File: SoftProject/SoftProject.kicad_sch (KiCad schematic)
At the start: 37 parts, among them J1 USB_B_Micro, Q1 2N2219, Q2 2N2219, SW1 SW_Push, SW2 SW_Push, U1 ESP32-S2-WROVER, U2 AMS1117, U3 CP2102N-Axx-xQFN28

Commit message: Finished schematic
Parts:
- added J2: Conn_01x21_Pin, symbol Connector:Conn_01x21_Pin
- added J4: Conn_01x19_Pin, symbol Connector:Conn_01x19_Pin
- added R13: R, symbol Device:R
- added R14, R15, R16, R17: 0, symbol Device:R
- C1, C14, C4, C7, C8, C9: value 0.1u -> 0.1uF
- C10, C2, C5, C6: value 10u -> 10uF
- C11, C12: value 22p -> 22pF
- C13: value 4.7u -> 4.7uF
- C3: value 1u -> 1uF
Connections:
- net +3.3V: now also J2.1 (Pin_1)
- net +5V: now also J2.20 (Pin_20)
- net CHIP_PU: now also J4.2 (Pin_2), R16.2
- net EN_Auto: now also R16.1
- net GND: now also J2.21 (Pin_21), J4.1 (Pin_1), J4.19 (Pin_19), R13.2
- net GPIO0: now also J2.2 (Pin_2), R17.2
- net GPIO1: now also J2.3 (Pin_3)
- net GPIO10: now also J2.12 (Pin_12)
- net GPIO11: now also J2.13 (Pin_13)
- net GPIO12: now also J2.14 (Pin_14)
- net GPIO13: now also J2.15 (Pin_15)
- net GPIO14: now also J2.16 (Pin_16)
- net GPIO15: now also J2.17 (Pin_17)
- net GPIO16: now also J2.18 (Pin_18)
- net GPIO17: now also J2.19 (Pin_19)
- net GPIO2: now also J2.4 (Pin_4)
- net GPIO3: now also J2.5 (Pin_5)
- net GPIO4: now also J2.6 (Pin_6)
- net GPIO5: now also J2.7 (Pin_7)
- net GPIO6: now also J2.8 (Pin_8)
- net GPIO7: now also J2.9 (Pin_9)
- net GPIO8: now also J2.10 (Pin_10)
- net GPIO9: now also J2.11 (Pin_11)
- net IO0_Auto: now also R17.1
- net RXD_CP: now also J4.5 (Pin_5), R15.2
- net TXD_CP: now also J4.6 (Pin_6), R14.2
- net USB_DN: now also U1.22 (USB_D-)
- net USB_DP: now also U1.23 (USB_D+)
- net at U3.11 (~{SUSPEND}): now also R13.1
- net GPIO21: now reaches U1.24 (IO21)
- net GPIO21: now also J4.18 (Pin_18)
- net GPIO26: now reaches U1.25 (IO26)
- net GPIO26: now also J4.17 (Pin_17)
- net GPIO33: now reaches U1.27 (IO33)
- net GPIO33: now also J4.16 (Pin_16)
- net GPIO34: now reaches U1.28 (IO34)
- net GPIO34: now also J4.15 (Pin_15)
- net GPIO35: now reaches U1.29 (IO35)
- net GPIO35: now also J4.14 (Pin_14)
- net GPIO36: now reaches U1.30 (IO36)
- net GPIO36: now also J4.13 (Pin_13)
- net GPIO37: now reaches U1.31 (IO37)
- net GPIO37: now also J4.12 (Pin_12)
- net GPIO38: now reaches U1.32 (IO38)
- net GPIO38: now also J4.11 (Pin_11)
- net GPIO39: now reaches U1.33 (IO39)
- net GPIO39: now also J4.10 (Pin_10)
- net GPIO40: now reaches U1.34 (IO40)
- net GPIO40: now also J4.9 (Pin_9)
- net GPIO41: now reaches U1.35 (IO41)
- net GPIO41: now also J4.8 (Pin_8)
- net GPIO42: now reaches U1.36 (IO42)
- net GPIO42: now also J4.7 (Pin_7)
- net TXD: now reaches U1.37 (TXD0)
- net TXD: now also R15.1
- net RXD: now reaches U1.38 (RXD0)
- net RXD: now also R14.1
- net GPIO45: now reaches U1.39 (IO45)
- net GPIO45: now also J4.4 (Pin_4)
- net GPIO46: now reaches U1.40 (IO46)
- net GPIO46: now also J4.3 (Pin_3)
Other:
- moved on the sheet: C1, C10, C11, C12, C13, C14, C2, C3, C4, C5, C6, C7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

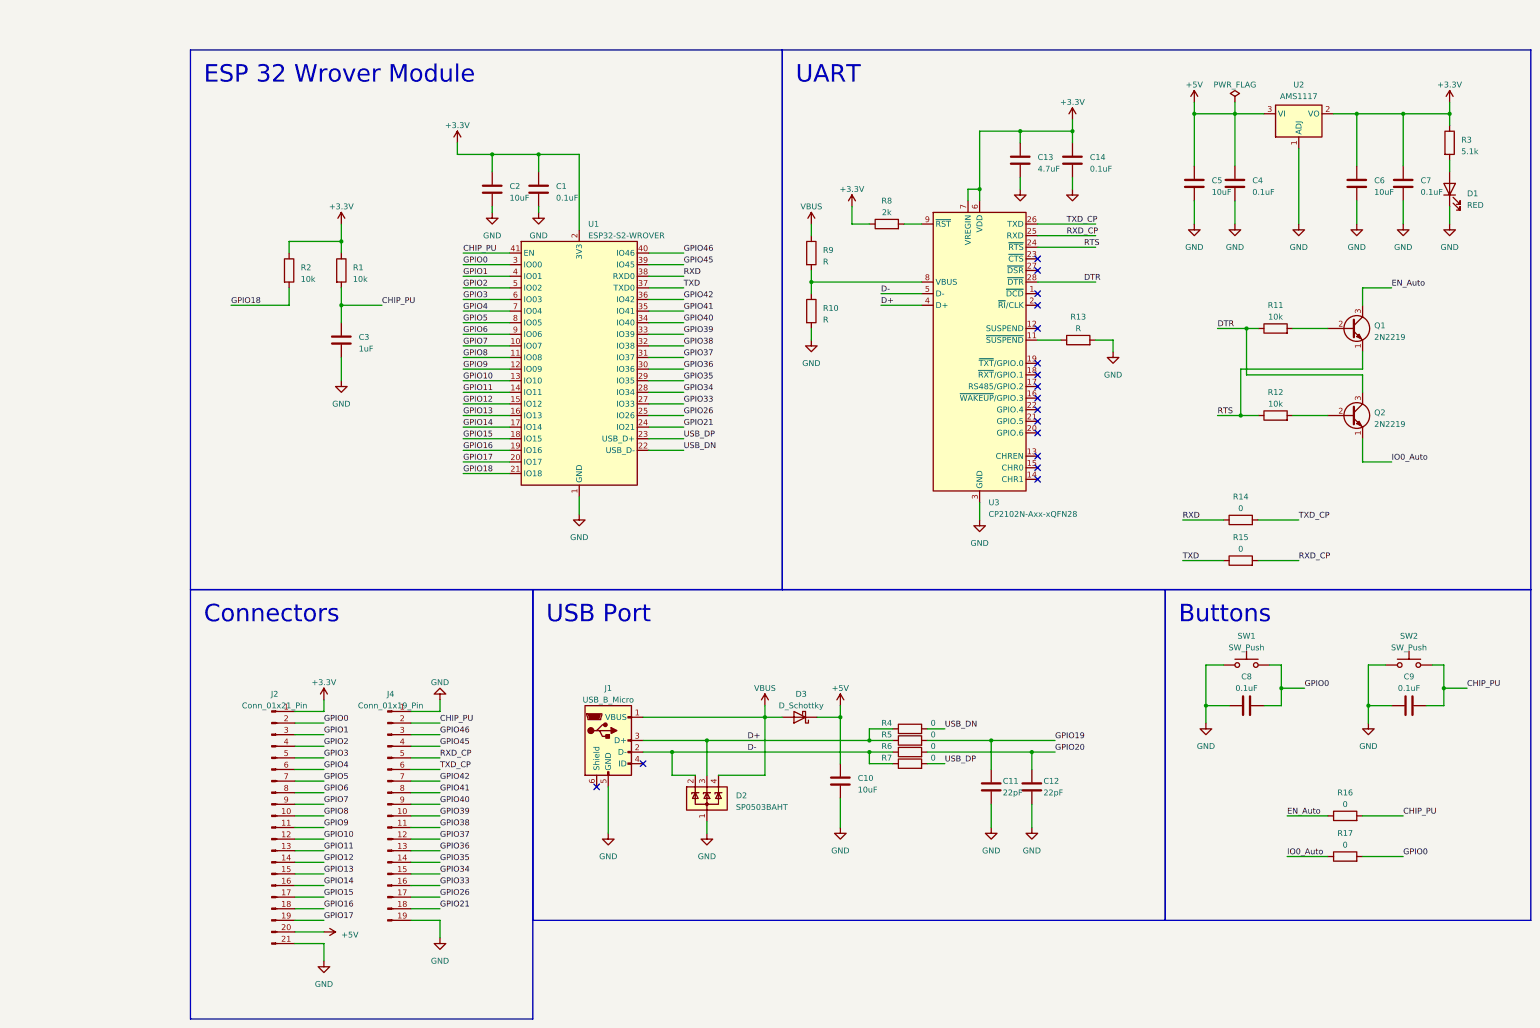
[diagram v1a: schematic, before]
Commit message: Added some footprints
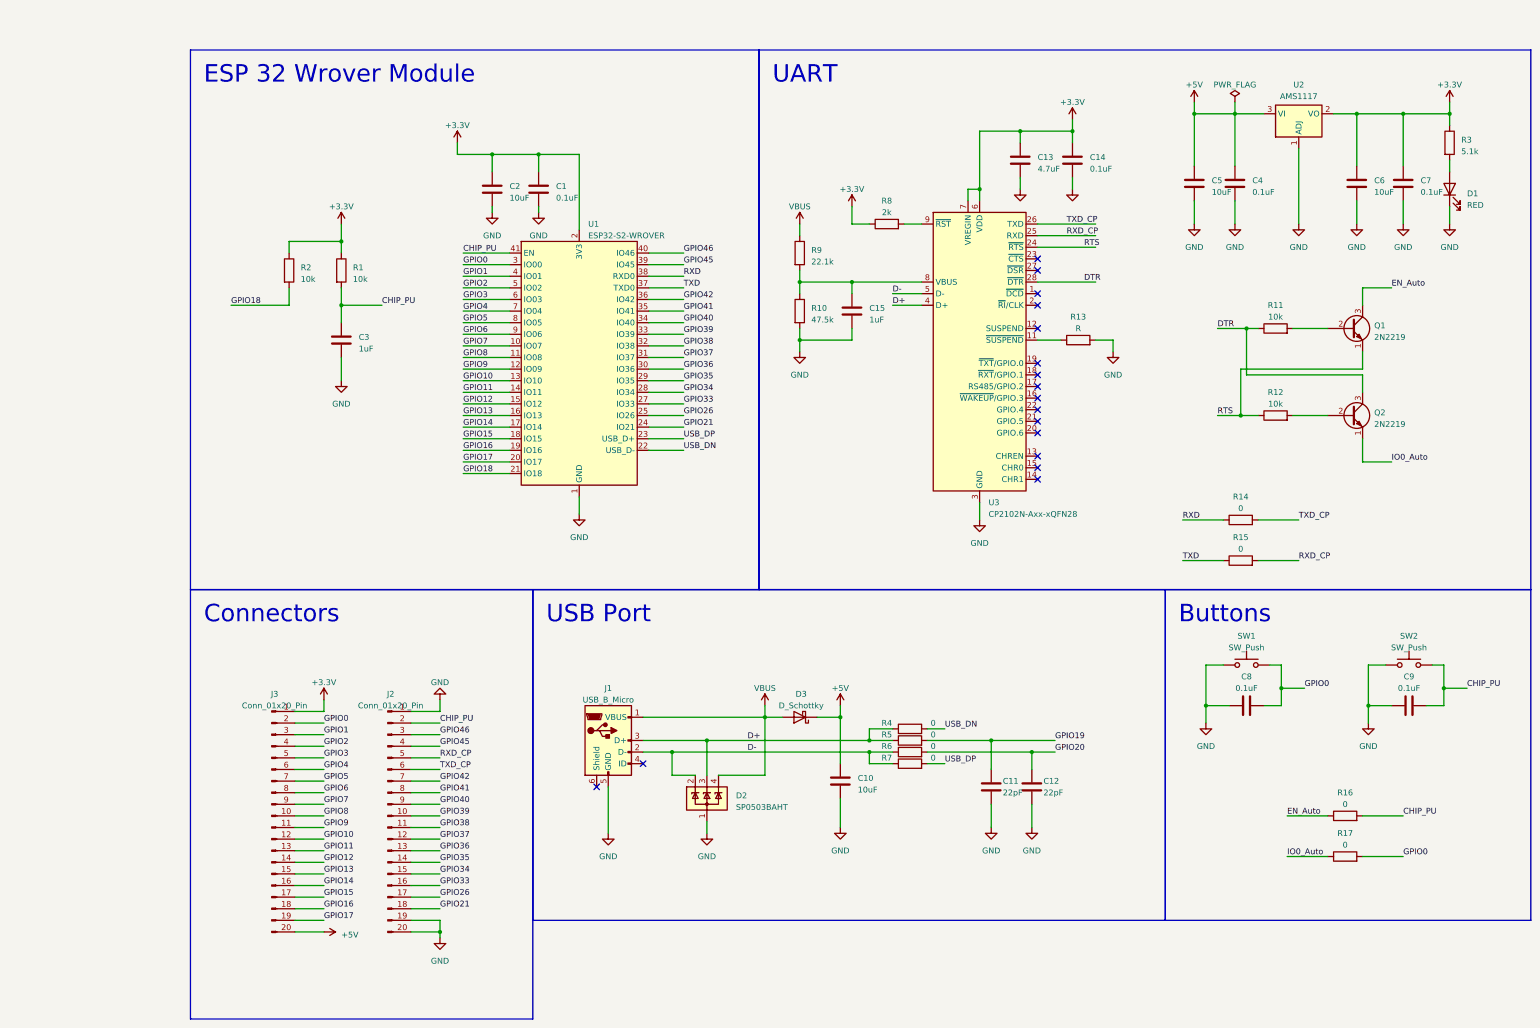
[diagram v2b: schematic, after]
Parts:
- removed J2: Conn_01x21_Pin, symbol Connector:Conn_01x21_Pin
- removed J4: Conn_01x19_Pin, symbol Connector:Conn_01x19_Pin
- added C15: 1uF, symbol Device:C
- added J2: Conn_01x20_Pin, Connector_PinHeader_2.54mm:PinHeader_1x20_P2.54mm_Vertical, symbol Connector:Conn_01x20_Pin
- added J3: Conn_01x20_Pin, Connector_PinSocket_2.54mm:PinSocket_1x20_P2.54mm_Vertical, symbol Connector:Conn_01x20_Pin
- J1: footprint (none) -> Connector_USB:USB_Micro-B_Wuerth_629105150521
- R10: value R -> 47.5k
- R9: value R -> 22.1k
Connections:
- net +3.3V: now also J3.1 (Pin_1)
- net +5V: now also J3.20 (Pin_20)
- net CHIP_PU: now also J2.2 (Pin_2)
- net GND: now also C15.2, J2.1 (Pin_1), J2.19 (Pin_19), J2.20 (Pin_20)
- net GPIO0: now also J3.2 (Pin_2)
- net GPIO1: now also J3.3 (Pin_3)
- net GPIO10: now also J3.12 (Pin_12)
- net GPIO11: now also J3.13 (Pin_13)
- net GPIO12: now also J3.14 (Pin_14)
- net GPIO13: now also J3.15 (Pin_15)
- net GPIO14: now also J3.16 (Pin_16)
- net GPIO15: now also J3.17 (Pin_17)
- net GPIO16: now also J3.18 (Pin_18)
- net GPIO17: now also J3.19 (Pin_19)
- net GPIO2: now also J3.4 (Pin_4)
- net GPIO21: now also J2.18 (Pin_18)
- net GPIO26: now also J2.17 (Pin_17)
- net GPIO3: now also J3.5 (Pin_5)
- net GPIO33: now also J2.16 (Pin_16)
- net GPIO34: now also J2.15 (Pin_15)
- net GPIO35: now also J2.14 (Pin_14)
- net GPIO36: now also J2.13 (Pin_13)
- net GPIO37: now also J2.12 (Pin_12)
- net GPIO38: now also J2.11 (Pin_11)
- net GPIO39: now also J2.10 (Pin_10)
- net GPIO4: now also J3.6 (Pin_6)
- net GPIO40: now also J2.9 (Pin_9)
- net GPIO41: now also J2.8 (Pin_8)
- net GPIO42: now also J2.7 (Pin_7)
- net GPIO45: now also J2.4 (Pin_4)
- net GPIO46: now also J2.3 (Pin_3)
- net GPIO5: now also J3.7 (Pin_7)
- net GPIO6: now also J3.8 (Pin_8)
- net GPIO7: now also J3.9 (Pin_9)
- net GPIO8: now also J3.10 (Pin_10)
- net GPIO9: now also J3.11 (Pin_11)
- net RXD_CP: now also J2.5 (Pin_5)
- net TXD_CP: now also J2.6 (Pin_6)
- net at R10.1, R9.2, U3.8 (VBUS): now also C15.1
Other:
- moved on the sheet: R10, R9

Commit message: Finished layout. Started routing.
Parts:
- removed J2: Conn_01x20_Pin, Connector_PinHeader_2.54mm:PinHeader_1x20_P2.54mm_Vertical, symbol Connector:Conn_01x20_Pin
- removed J3: Conn_01x20_Pin, Connector_PinSocket_2.54mm:PinSocket_1x20_P2.54mm_Vertical, symbol Connector:Conn_01x20_Pin
- removed R4, R7: 0, symbol Device:R
- added H1, H2, H3, H4: MountingHole, MountingHole:MountingHole_2.2mm_M2, symbol Mechanical:MountingHole
- added J3, J4: Conn_01x20_Socket, Connector_PinSocket_2.54mm:PinSocket_1x20_P2.54mm_Vertical, symbol Connector:Conn_01x20_Socket
- C1, C11, C12, C14, C15, C3, C4, C7, C8, C9: footprint (none) -> Capacitor_SMD:C_0402_1005Metric
- C10, C2, C5, C6: footprint (none) -> Capacitor_SMD:C_0805_2012Metric
- C13: footprint (none) -> Capacitor_SMD:C_0603_1608Metric
- D1: footprint (none) -> LED_SMD:LED_0603_1608Metric
- D3: footprint (none) -> Diode_SMD:D_SOD-323
- Q1, Q2: footprint Package_TO_SOT_THT:TO-39-3 -> Package_TO_SOT_SMD:SOT-23
- R1, R10, R11, R12, R14, R15, R16, R17, R2, R3, R5, R6, R8, R9: footprint (none) -> Resistor_SMD:R_0402_1005Metric
- R13: value R -> 10k; footprint (none) -> Resistor_SMD:R_0402_1005Metric
- SW1, SW2: footprint (none) -> Button_Switch_SMD:SW_SPST_B3U-1000P
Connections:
- net USB_DN is gone; now on net DN: U1.22 (USB_D-)
- net USB_DP is gone; now on net DP: U1.23 (USB_D+)
- net +3.3V: now also J4.1 (Pin_1)
- net +5V: now also J4.20 (Pin_20)
- net CHIP_PU: now also J3.2 (Pin_2)
- net GND: now also J3.1 (Pin_1), J3.19 (Pin_19), J3.20 (Pin_20)
- net GPIO0: now also J4.2 (Pin_2)
- net GPIO1: now also J4.3 (Pin_3)
- net GPIO10: now also J4.12 (Pin_12)
- net GPIO11: now also J4.13 (Pin_13)
- net GPIO12: now also J4.14 (Pin_14)
- net GPIO13: now also J4.15 (Pin_15)
- net GPIO14: now also J4.16 (Pin_16)
- net GPIO15: now also J4.17 (Pin_17)
- net GPIO16: now also J4.18 (Pin_18)
- net GPIO17: now also J4.19 (Pin_19)
- net GPIO2: now also J4.4 (Pin_4)
- net GPIO21: now also J3.18 (Pin_18)
- net GPIO26: now also J3.17 (Pin_17)
- net GPIO3: now also J4.5 (Pin_5)
- net GPIO33: now also J3.16 (Pin_16)
- net GPIO34: now also J3.15 (Pin_15)
- net GPIO35: now also J3.14 (Pin_14)
- net GPIO36: now also J3.13 (Pin_13)
- net GPIO37: now also J3.12 (Pin_12)
- net GPIO38: now also J3.11 (Pin_11)
- net GPIO39: now also J3.10 (Pin_10)
- net GPIO4: now also J4.6 (Pin_6)
- net GPIO40: now also J3.9 (Pin_9)
- net GPIO41: now also J3.8 (Pin_8)
- net GPIO42: now also J3.7 (Pin_7)
- net GPIO45: now also J3.4 (Pin_4)
- net GPIO46: now also J3.3 (Pin_3)
- net GPIO5: now also J4.7 (Pin_7)
- net GPIO6: now also J4.8 (Pin_8)
- net GPIO7: now also J4.9 (Pin_9)
- net GPIO8: now also J4.10 (Pin_10)
- net GPIO9: now also J4.11 (Pin_11)
- net RXD: now also J3.5 (Pin_5)
- net TXD: now also J3.6 (Pin_6)
- net GPIO19 renamed DP
- net GPIO20 renamed DN

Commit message: Finished ESP32Board
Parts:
- C1, C14, C4, C7, C8, C9: JLCPCB Part Number (none) -> C105883
- C10, C2, C5, C6: JLCPCB Part Number (none) -> C440198
- C11, C12: JLCPCB Part Number (none) -> C147430
- C13: JLCPCB Part Number (none) -> C2171286
- C15, C3: JLCPCB Part Number (none) -> C326568
- D1: JLCPCB Part Number (none) -> C84263
- D2: JLCPCB Part Number (none) -> C3040626
- D3: JLCPCB Part Number (none) -> C116158
- J1: JLCPCB Part Number (none) -> C9900016360
- Q1, Q2: JLCPCB Part Number (none) -> C475630
- R1, R11, R12, R13, R2: JLCPCB Part Number (none) -> C409612
- R10: JLCPCB Part Number (none) -> C319604
- R14, R15, R16, R17, R5, R6: JLCPCB Part Number (none) -> C279984
- R3: JLCPCB Part Number (none) -> C147799
- R8: JLCPCB Part Number (none) -> C409711
- R9: JLCPCB Part Number (none) -> C325588
- SW1, SW2: footprint Button_Switch_SMD:SW_SPST_B3U-1000P -> B3U-1000P:B3U-1000P; JLCPCB Part Number (none) -> C231329
- U1: JLCPCB Part Number (none) -> C701333
- U2: JLCPCB Part Number (none) -> C369933
- U3: JLCPCB Part Number (none) -> C964632

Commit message: Finished and ordered PCB
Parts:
- J1: footprint Connector_USB:USB_Micro-B_Wuerth_629105150521 -> Connector_USB:USB_Micro-B_Molex-105017-0001; JLCPCB Part Number C9900016360 -> C136000
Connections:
- net DTR: now also Q2.1 (E); no longer Q2.3 (C)
- net IO0_Auto: now also Q2.3 (C); no longer Q2.1 (E)
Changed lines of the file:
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@@
       (effects (font (size 1.27 1.27)))
     )
-    (property "Footprint" "Connector_USB:USB_Micro-B_Wuerth_629105150521" (at 154.94 191.77 0)
+    (property "Footprint" "Connector_USB:USB_Micro-B_Molex-105017-0001" (at 154.94 191.77 0)
       (effects (font (size 1.27 1.27)) hide)
     )
@@
       (effects (font (size 1.27 1.27)) hide)
     )
-    (property "JLCPCB Part Number" "C9900016360" (at 151.13 190.5 0)
+    (property "JLCPCB Part Number" "C136000" (at 151.13 190.5 0)
       (effects (font (size 1.27 1.27)) hide)
     )
@@
     )
   )
-  (symbol (lib_id "Transistor_BJT:2N2219") (at 313.69 119.38 0) (unit 1)
-    (in_bom yes) (on_board yes) (dnp no) (fields_autoplaced)
-    (property "Reference" "Q2" (at 318.77 118.745 0)
-      (effects (font (size 1.27 1.27)) (justify left))
-    )
-    (property "Value" "2N2219" (at 318.77 121.285 0)
-      (effects (font (size 1.27 1.27)) (justify left))
-    )
-    (property "Footprint" "Package_TO_SOT_SMD:SOT-23" (at 318.77 121.285 0)
+  (symbol (lib_id "Transistor_BJT:2N2219") (at 313.69 119.38 0) (mirror x) (unit 1)
+    (in_bom yes) (on_board yes) (dnp no)
+    (property "Reference" "Q2" (at 318.77 120.015 0)
+      (effects (font (size 1.27 1.27)) (justify left))
+    )
+    (property "Value" "2N2219" (at 318.77 117.475 0)
+      (effects (font (size 1.27 1.27)) (justify left))
+    )
+    (property "Footprint" "Package_TO_SOT_SMD:SOT-23" (at 318.77 117.475 0)
       (effects (font (size 1.27 1.27) italic) (justify left) hide)
     )
